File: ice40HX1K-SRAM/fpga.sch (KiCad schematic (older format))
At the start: 16 parts

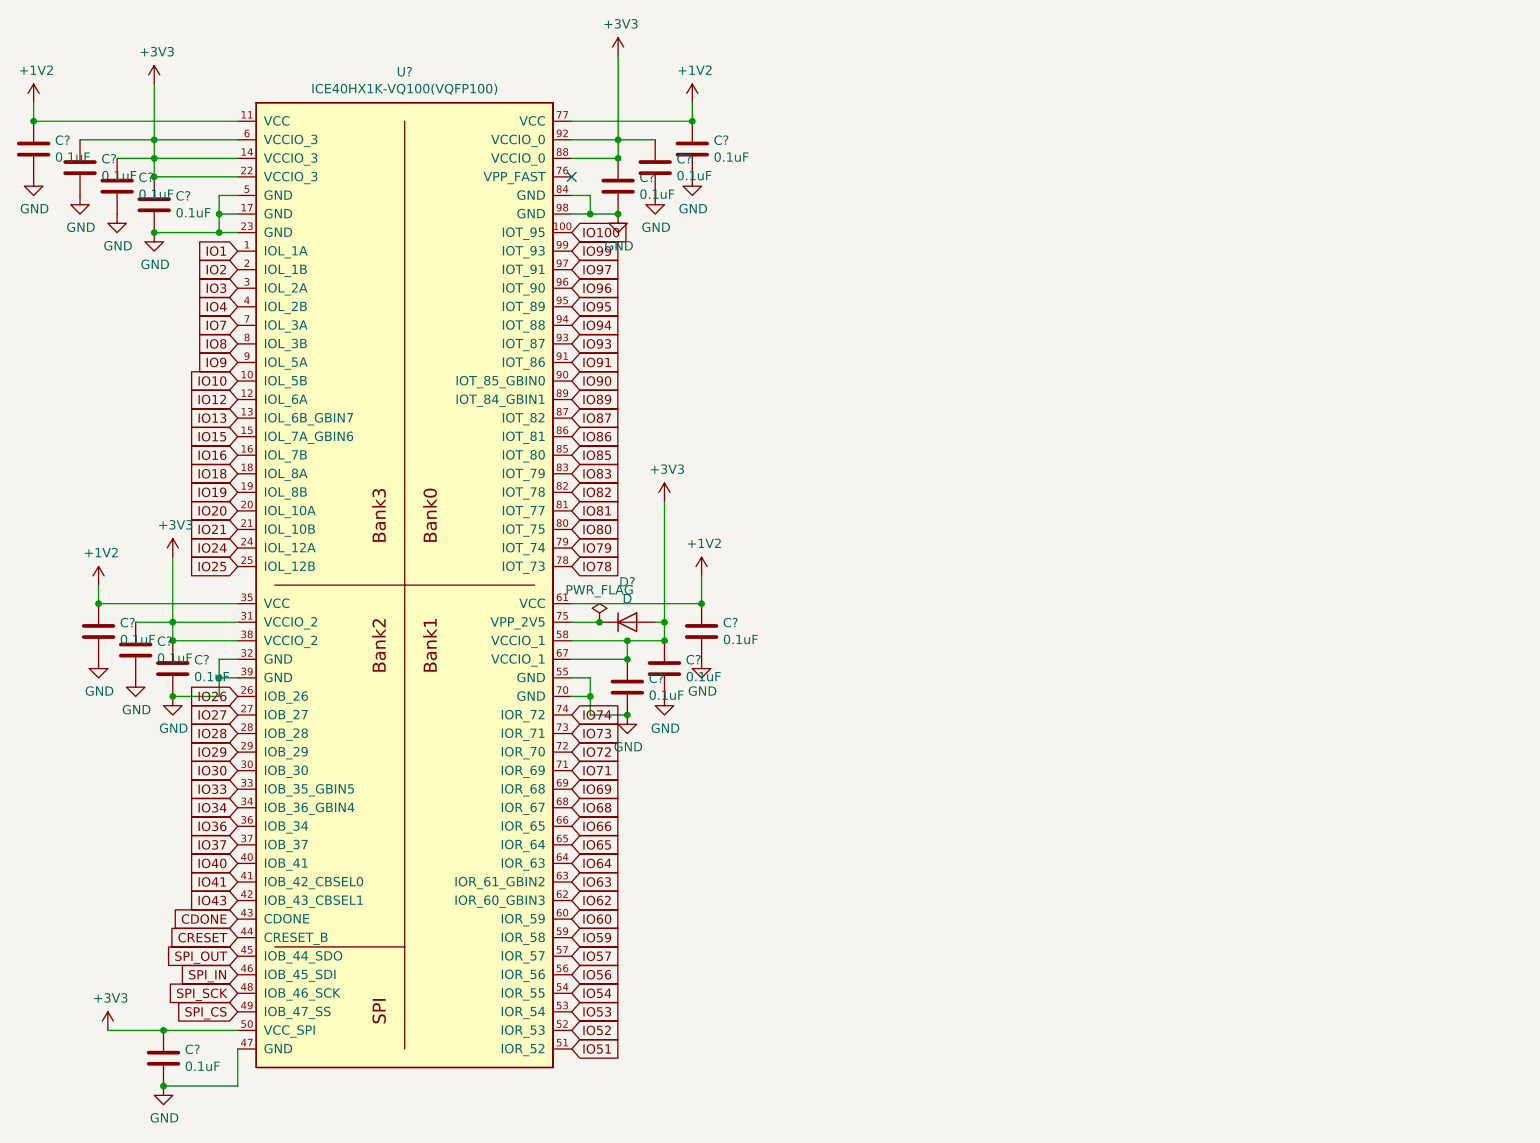
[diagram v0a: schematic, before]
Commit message: wiring FPGA nRF52 and ATSAMD11
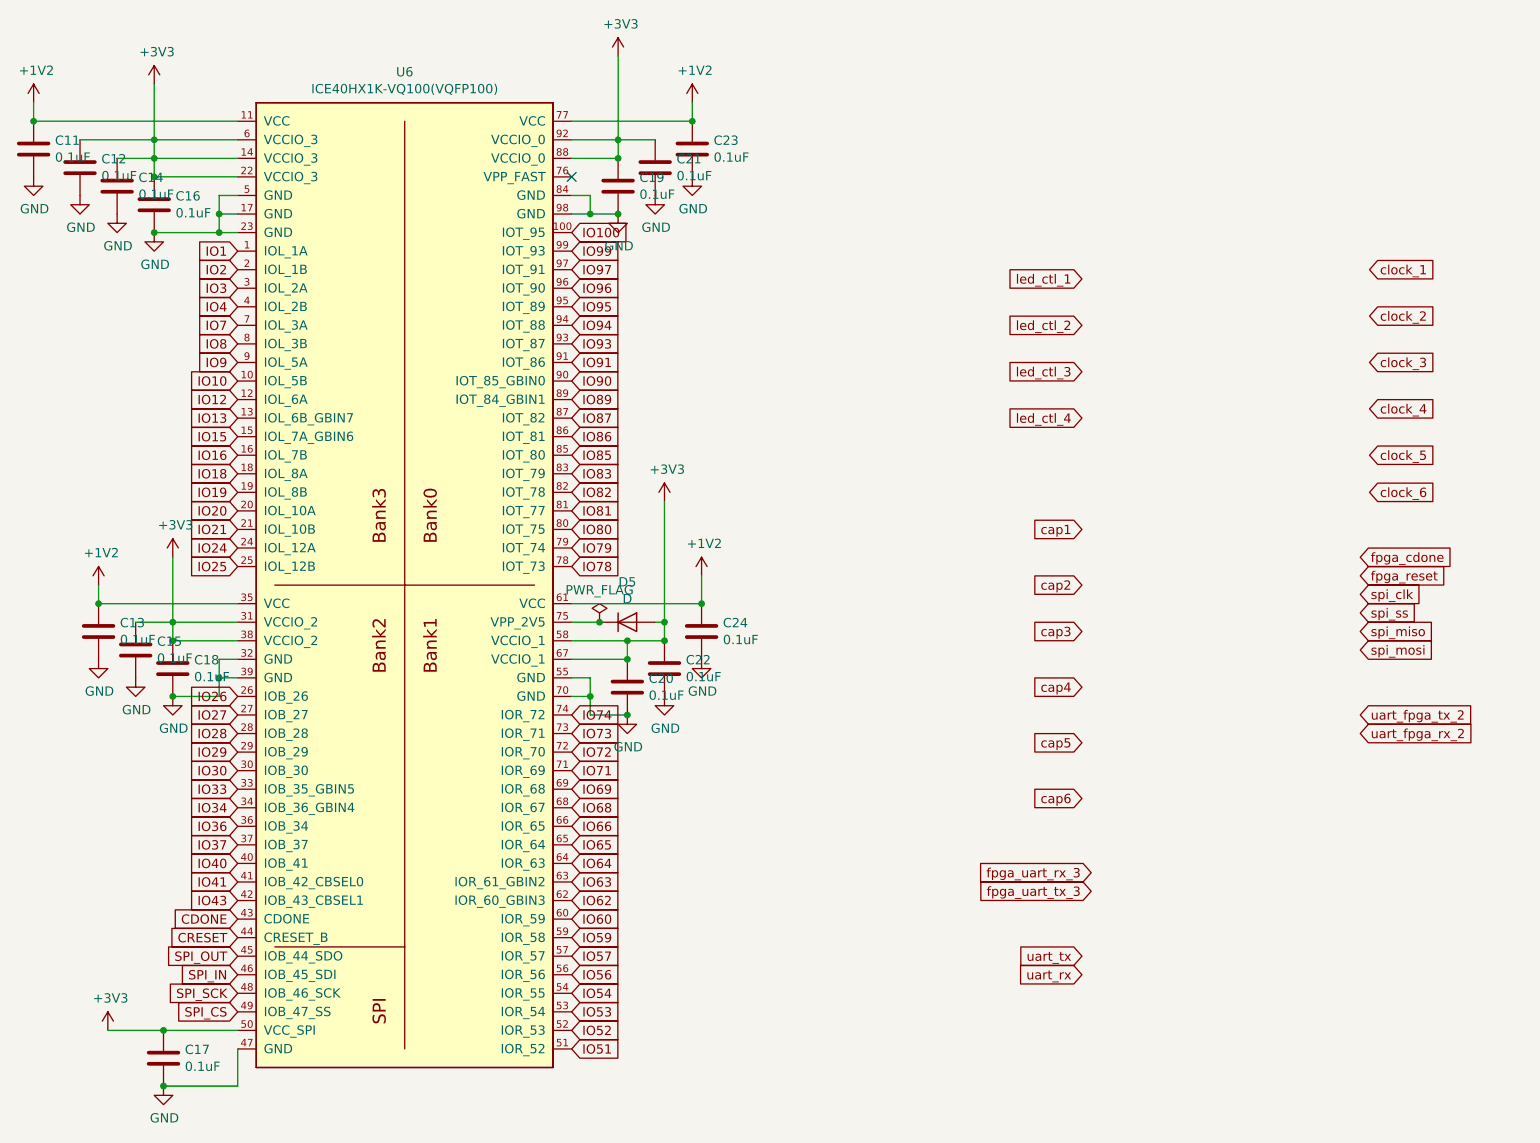
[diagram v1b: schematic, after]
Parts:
- gave numbers to parts that had none: 16

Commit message: wiring FPGA
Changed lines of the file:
@@
 Text GLabel 7400 6000 0    50   Input ~ 0
 uart_rx
+Text GLabel 7400 6000 2    50   Input ~ 0
+IO54
+Text GLabel 7400 5900 2    50   Input ~ 0
+IO56
+Text GLabel 7450 5550 2    50   Input ~ 0
+IO57
+Text GLabel 7450 5450 2    50   Input ~ 0
+IO59
+Text GLabel 8900 4700 0    50   Input ~ 0
+IO60
+Text GLabel 8900 4600 0    50   Input ~ 0
+IO64
+Text GLabel 8950 2200 0    50   Input ~ 0
+IO62
+Text GLabel 8950 3400 0    50   Input ~ 0
+IO63
+Text GLabel 8950 2450 0    50   Input ~ 0
+IO65
+Text GLabel 8950 2700 0    50   Input ~ 0
+IO66
+Text GLabel 8950 2950 0    50   Input ~ 0
+IO68
+Text GLabel 8950 3200 0    50   Input ~ 0
+IO69
+Text GLabel 7400 3000 2    50   Input ~ 0
+IO71
+Text GLabel 7400 2750 2    50   Input ~ 0
+IO72
+Text GLabel 7400 2500 2    50   Input ~ 0
+IO73
+Text GLabel 7400 2250 2    50   Input ~ 0
+IO74
+Text GLabel 8900 3750 0    50   Input ~ 0
+CDONE
+Text GLabel 8900 3850 0    50   Input ~ 0
+CRESET
+Text GLabel 8900 4250 0    50   Input ~ 0
+SPI_OUT
+Text GLabel 8900 4150 0    50   Input ~ 0
+SPI_IN
+Text GLabel 8900 3950 0    50   Input ~ 0
+SPI_SCK
+Text GLabel 8900 4050 0    50   Input ~ 0
+SPI_CS
+Text GLabel 7400 5050 2    50   Input ~ 0
+IO94
+Text GLabel 7400 4750 2    50   Input ~ 0
+IO95
+Text GLabel 7400 4450 2    50   Input ~ 0
+IO96
+Text GLabel 7400 4150 2    50   Input ~ 0
+IO97
+Text GLabel 7400 3900 2    50   Input ~ 0
+IO99
+Text GLabel 7400 3600 2    50   Input ~ 0
+IO100
 $EndSCHEMATC

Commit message: wiring FPGA
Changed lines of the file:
@@
 Text GLabel 7400 5050 0    50   Input ~ 0
 cap6
-Text GLabel 8950 2200 2    50   Input ~ 0
+Text GLabel 9050 2200 2    50   Input ~ 0
 clock_1
-Text GLabel 8950 2450 2    50   Input ~ 0
+Text GLabel 9050 2450 2    50   Input ~ 0
 clock_2
-Text GLabel 8950 2700 2    50   Input ~ 0
+Text GLabel 9050 2700 2    50   Input ~ 0
 clock_3
-Text GLabel 8950 2950 2    50   Input ~ 0
+Text GLabel 9050 2950 2    50   Input ~ 0
 clock_4
-Text GLabel 8950 3200 2    50   Input ~ 0
+Text GLabel 9050 3200 2    50   Input ~ 0
 clock_5
-Text GLabel 8950 3400 2    50   Input ~ 0
+Text GLabel 9050 3400 2    50   Input ~ 0
 clock_6
-Text GLabel 8900 3950 2    50   Input ~ 0
+Text GLabel 9000 3950 2    50   Input ~ 0
 spi_clk
-Text GLabel 8900 4050 2    50   Input ~ 0
+Text GLabel 9000 4050 2    50   Input ~ 0
 spi_ss
-Text GLabel 8900 4150 2    50   Input ~ 0
+Text GLabel 9000 4150 2    50   Input ~ 0
 spi_miso
-Text GLabel 8900 4250 2    50   Input ~ 0
+Text GLabel 9000 4250 2    50   Input ~ 0
 spi_mosi
-Text GLabel 8900 3850 2    50   Input ~ 0
+Text GLabel 9000 3850 2    50   Input ~ 0
 fpga_reset
-Text GLabel 8900 3750 2    50   Input ~ 0
+Text GLabel 9000 3750 2    50   Input ~ 0
 fpga_cdone
 Text GLabel 7450 5450 0    50   Input ~ 0
@@
 Text GLabel 7450 5550 0    50   Input ~ 0
 fpga_uart_tx_3
-Text GLabel 8900 4600 2    50   Input ~ 0
+Text GLabel 9000 4600 2    50   Input ~ 0
 uart_fpga_tx_2
-Text GLabel 8900 4700 2    50   Input ~ 0
+Text GLabel 9000 4700 2    50   Input ~ 0
 uart_fpga_rx_2
 Text GLabel 7400 5900 0    50   Input ~ 0
@@
 Text GLabel 7400 6000 0    50   Input ~ 0
 uart_rx
-Text GLabel 7400 6000 2    50   Input ~ 0
+Text GLabel 7500 6000 2    50   Input ~ 0
 IO54
-Text GLabel 7400 5900 2    50   Input ~ 0
+Text GLabel 7500 5900 2    50   Input ~ 0
 IO56
-Text GLabel 7450 5550 2    50   Input ~ 0
+Text GLabel 7550 5550 2    50   Input ~ 0
 IO57
-Text GLabel 7450 5450 2    50   Input ~ 0
+Text GLabel 7550 5450 2    50   Input ~ 0
 IO59
 Text GLabel 8900 4700 0    50   Input ~ 0
@@
 Text GLabel 8950 3200 0    50   Input ~ 0
 IO69
-Text GLabel 7400 3000 2    50   Input ~ 0
+Text GLabel 7500 3000 2    50   Input ~ 0
 IO71
-Text GLabel 7400 2750 2    50   Input ~ 0
+Text GLabel 7500 2750 2    50   Input ~ 0
 IO72
-Text GLabel 7400 2500 2    50   Input ~ 0
+Text GLabel 7500 2500 2    50   Input ~ 0
 IO73
-Text GLabel 7400 2250 2    50   Input ~ 0
+Text GLabel 7500 2250 2    50   Input ~ 0
 IO74
 Text GLabel 8900 3750 0    50   Input ~ 0
@@
 Text GLabel 8900 4050 0    50   Input ~ 0
 SPI_CS
-Text GLabel 7400 5050 2    50   Input ~ 0
+Text GLabel 7500 5050 2    50   Input ~ 0
 IO94
-Text GLabel 7400 4750 2    50   Input ~ 0
+Text GLabel 7500 4750 2    50   Input ~ 0
 IO95
-Text GLabel 7400 4450 2    50   Input ~ 0
+Text GLabel 7500 4450 2    50   Input ~ 0
 IO96
-Text GLabel 7400 4150 2    50   Input ~ 0
+Text GLabel 7500 4150 2    50   Input ~ 0
 IO97
-Text GLabel 7400 3900 2    50   Input ~ 0
+Text GLabel 7500 3900 2    50   Input ~ 0
 IO99
-Text GLabel 7400 3600 2    50   Input ~ 0
+Text GLabel 7500 3600 2    50   Input ~ 0
 IO100
+Wire Wire Line
+	7400 2250 7500 2250
+Wire Wire Line
+	7400 2500 7500 2500
+Wire Wire Line
+	7400 2750 7500 2750
+Wire Wire Line
+	7400 3000 7500 3000
+Wire Wire Line
+	7450 5450 7550 5450
+Wire Wire Line
+	7450 5550 7550 5550
+Wire Wire Line
+	7400 5900 7500 5900
+Wire Wire Line
+	7400 6000 7500 6000
+Wire Wire Line
+	7400 3600 7500 3600
+Wire Wire Line
+	7400 3900 7500 3900
+Wire Wire Line
+	7400 4150 7500 4150
+Wire Wire Line
+	7400 4450 7500 4450
+Wire Wire Line
+	7400 4750 7500 4750
+Wire Wire Line
+	7400 5050 7500 5050
+Wire Wire Line
+	8950 2200 9050 2200
+Wire Wire Line
+	8950 2450 9050 2450
+Wire Wire Line
+	8950 2700 9050 2700
+Wire Wire Line
+	8950 2950 9050 2950
+Wire Wire Line
+	8950 3200 9050 3200
+Wire Wire Line
+	8950 3400 9050 3400
+Wire Wire Line
+	8900 3750 9000 3750
+Wire Wire Line
+	8900 3850 9000 3850
+Wire Wire Line
+	8900 3950 9000 3950
+Wire Wire Line
+	8900 4050 9000 4050
+Wire Wire Line
+	8900 4150 9000 4150
+Wire Wire Line
+	8900 4250 9000 4250
+Wire Wire Line
+	8900 4600 9000 4600
+Wire Wire Line
+	8900 4700 9000 4700
 $EndSCHEMATC

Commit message: wiring FPGA
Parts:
- C11, C12, C13, C14, C15, C16, C17, C18, C19, C20, C21, C22, C23, C24: footprint Capacitor_SMD:C_0805_2012Metric -> Capacitor_SMD:C_0402_1005Metric
- D5: value D -> CDBU05
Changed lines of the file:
@@
 F 0 "C11" H 1865 1596 50  0000 L CNN
 F 1 "0.1uF" H 1865 1505 50  0000 L CNN
-F 2 "Capacitor_SMD:C_0805_2012Metric" H 1788 1400 50  0001 C CNN
+F 2 "Capacitor_SMD:C_0402_1005Metric" H 1788 1400 50  0001 C CNN
 F 3 "~" H 1750 1550 50  0001 C CNN
 	1    1750 1550
@@
 F 0 "C12" H 2115 1696 50  0000 L CNN
 F 1 "0.1uF" H 2115 1605 50  0000 L CNN
-F 2 "Capacitor_SMD:C_0805_2012Metric" H 2038 1500 50  0001 C CNN
+F 2 "Capacitor_SMD:C_0402_1005Metric" H 2038 1500 50  0001 C CNN
 F 3 "~" H 2000 1650 50  0001 C CNN
 	1    2000 1650
@@
 F 0 "C14" H 2315 1796 50  0000 L CNN
 F 1 "0.1uF" H 2315 1705 50  0000 L CNN
-F 2 "Capacitor_SMD:C_0805_2012Metric" H 2238 1600 50  0001 C CNN
+F 2 "Capacitor_SMD:C_0402_1005Metric" H 2238 1600 50  0001 C CNN
 F 3 "~" H 2200 1750 50  0001 C CNN
 	1    2200 1750
@@
 F 0 "C16" H 2515 1896 50  0000 L CNN
 F 1 "0.1uF" H 2515 1805 50  0000 L CNN
-F 2 "Capacitor_SMD:C_0805_2012Metric" H 2438 1700 50  0001 C CNN
+F 2 "Capacitor_SMD:C_0402_1005Metric" H 2438 1700 50  0001 C CNN
 F 3 "~" H 2400 1850 50  0001 C CNN
 	1    2400 1850
@@
 F 0 "C13" H 2215 4196 50  0000 L CNN
 F 1 "0.1uF" H 2215 4105 50  0000 L CNN
-F 2 "Capacitor_SMD:C_0805_2012Metric" H 2138 4000 50  0001 C CNN
+F 2 "Capacitor_SMD:C_0402_1005Metric" H 2138 4000 50  0001 C CNN
 F 3 "~" H 2100 4150 50  0001 C CNN
 	1    2100 4150
@@
 F 0 "C15" H 2415 4296 50  0000 L CNN
 F 1 "0.1uF" H 2415 4205 50  0000 L CNN
-F 2 "Capacitor_SMD:C_0805_2012Metric" H 2338 4100 50  0001 C CNN
+F 2 "Capacitor_SMD:C_0402_1005Metric" H 2338 4100 50  0001 C CNN
 F 3 "~" H 2300 4250 50  0001 C CNN
 	1    2300 4250
@@
 F 0 "C18" H 2615 4396 50  0000 L CNN
 F 1 "0.1uF" H 2615 4305 50  0000 L CNN
-F 2 "Capacitor_SMD:C_0805_2012Metric" H 2538 4200 50  0001 C CNN
+F 2 "Capacitor_SMD:C_0402_1005Metric" H 2538 4200 50  0001 C CNN
 F 3 "~" H 2500 4350 50  0001 C CNN
 	1    2500 4350
@@
 F 0 "C19" H 5015 1796 50  0000 L CNN
 F 1 "0.1uF" H 5015 1705 50  0000 L CNN
-F 2 "Capacitor_SMD:C_0805_2012Metric" H 4938 1600 50  0001 C CNN
+F 2 "Capacitor_SMD:C_0402_1005Metric" H 4938 1600 50  0001 C CNN
 F 3 "~" H 4900 1750 50  0001 C CNN
 	1    4900 1750
@@
 F 0 "C21" H 5215 1696 50  0000 L CNN
 F 1 "0.1uF" H 5215 1605 50  0000 L CNN
-F 2 "Capacitor_SMD:C_0805_2012Metric" H 5138 1500 50  0001 C CNN
+F 2 "Capacitor_SMD:C_0402_1005Metric" H 5138 1500 50  0001 C CNN
 F 3 "~" H 5100 1650 50  0001 C CNN
 	1    5100 1650
@@
 F 0 "C23" H 5415 1596 50  0000 L CNN
 F 1 "0.1uF" H 5415 1505 50  0000 L CNN
-F 2 "Capacitor_SMD:C_0805_2012Metric" H 5338 1400 50  0001 C CNN
+F 2 "Capacitor_SMD:C_0402_1005Metric" H 5338 1400 50  0001 C CNN
 F 3 "~" H 5300 1550 50  0001 C CNN
 	1    5300 1550
@@
 F 0 "C20" H 5065 4496 50  0000 L CNN
 F 1 "0.1uF" H 5065 4405 50  0000 L CNN
-F 2 "Capacitor_SMD:C_0805_2012Metric" H 4988 4300 50  0001 C CNN
+F 2 "Capacitor_SMD:C_0402_1005Metric" H 4988 4300 50  0001 C CNN
 F 3 "~" H 4950 4450 50  0001 C CNN
 	1    4950 4450
@@
 F 0 "C22" H 5265 4396 50  0000 L CNN
 F 1 "0.1uF" H 5265 4305 50  0000 L CNN
-F 2 "Capacitor_SMD:C_0805_2012Metric" H 5188 4200 50  0001 C CNN
+F 2 "Capacitor_SMD:C_0402_1005Metric" H 5188 4200 50  0001 C CNN
 F 3 "~" H 5150 4350 50  0001 C CNN
 	1    5150 4350
@@
 F 0 "C24" H 5465 4196 50  0000 L CNN
 F 1 "0.1uF" H 5465 4105 50  0000 L CNN
-F 2 "Capacitor_SMD:C_0805_2012Metric" H 5388 4000 50  0001 C CNN
+F 2 "Capacitor_SMD:C_0402_1005Metric" H 5388 4000 50  0001 C CNN
 F 3 "~" H 5350 4150 50  0001 C CNN
 	1    5350 4150
@@
 F 0 "C17" H 2565 6496 50  0000 L CNN
 F 1 "0.1uF" H 2565 6405 50  0000 L CNN
-F 2 "Capacitor_SMD:C_0805_2012Metric" H 2488 6300 50  0001 C CNN
+F 2 "Capacitor_SMD:C_0402_1005Metric" H 2488 6300 50  0001 C CNN
 F 3 "~" H 2450 6450 50  0001 C CNN
 	1    2450 6450
@@
 AR Path="/5E63F9B5/5E65E568" Ref="D5"  Part="1"
 F 0 "D5" H 4950 4316 50  0000 C CNN
-F 1 "D" H 4950 4225 50  0000 C CNN
+F 1 "CDBU05" H 4950 4225 50  0000 C CNN
 F 2 "Capacitor_SMD:C_0603_1608Metric" H 4950 4100 50  0001 C CNN
 F 3 "~" H 4950 4100 50  0001 C CNN
